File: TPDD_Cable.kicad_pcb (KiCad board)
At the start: 2 copper layers, 10.6 x 12 mm, 5 parts, among them J1 Wire Solder Pads, J2 TPDD, Q1 DTA114EKA, Q2 DTA114EKA, Q3 DTA114EKA

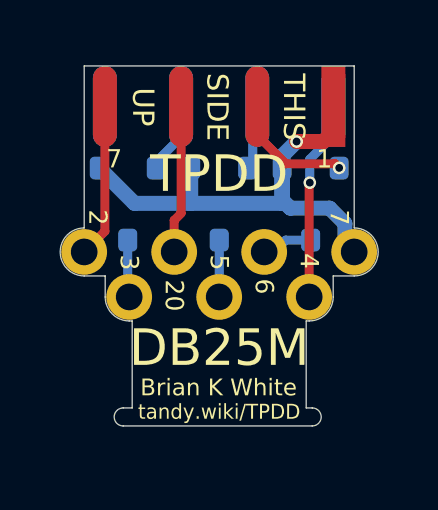
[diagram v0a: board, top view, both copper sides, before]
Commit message: pack v1 board tighter
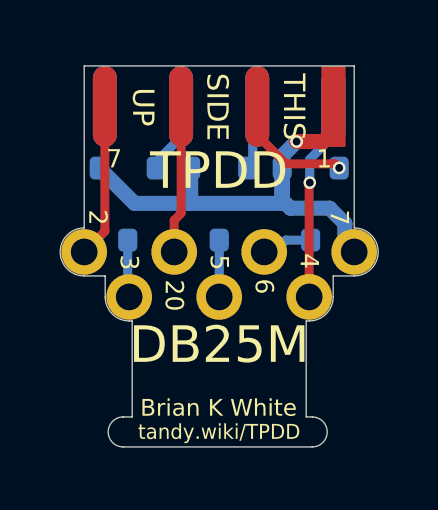
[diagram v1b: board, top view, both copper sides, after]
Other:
- board size 10.6 x 12 mm -> 10.6 x 12.7 mm
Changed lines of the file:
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@@
     (add_net /SG)
     (add_net /TX)
-    (add_net "Net-(J2-Pad8)")
   )
   (module 000_LOCAL:2-6-2_tpdd (layer Top)
@@
       (effects (font (size 1.2065 1.2065) (thickness 0.1016)) (justify right top mirror))
     )
+    (fp_line (start 0.762 1.524) (end 0.762 -1.516) (layer B.SilkS) (width 0.0508))
+    (fp_line (start -0.762 1.524) (end -0.762 -1.516) (layer B.SilkS) (width 0.0508))
+    (fp_line (start -0.762 1.524) (end 0.762 1.524) (layer B.SilkS) (width 0.0508))
     (fp_line (start -0.762 -1.516) (end 0.762 -1.516) (layer B.SilkS) (width 0.0508))
-    (fp_line (start -0.762 1.524) (end 0.762 1.524) (layer B.SilkS) (width 0.0508))
-    (fp_line (start -0.762 1.524) (end -0.762 -1.516) (layer B.SilkS) (width 0.0508))
-    (fp_line (start 0.762 1.524) (end 0.762 -1.516) (layer B.SilkS) (width 0.0508))
     (fp_text user %R (at 0 0) (layer B.Fab) hide
       (effects (font (size 0.5 0.5) (thickness 0.075)) (justify mirror))
@@
       (effects (font (size 1.2065 1.2065) (thickness 0.1016)) (justify right top mirror))
     )
+    (fp_line (start 0.762 1.524) (end 0.762 -1.516) (layer B.SilkS) (width 0.0508))
+    (fp_line (start -0.762 1.524) (end -0.762 -1.516) (layer B.SilkS) (width 0.0508))
+    (fp_line (start -0.762 1.524) (end 0.762 1.524) (layer B.SilkS) (width 0.0508))
     (fp_line (start -0.762 -1.516) (end 0.762 -1.516) (layer B.SilkS) (width 0.0508))
-    (fp_line (start -0.762 1.524) (end 0.762 1.524) (layer B.SilkS) (width 0.0508))
-    (fp_line (start -0.762 1.524) (end -0.762 -1.516) (layer B.SilkS) (width 0.0508))
-    (fp_line (start 0.762 1.524) (end 0.762 -1.516) (layer B.SilkS) (width 0.0508))
     (fp_text user %R (at 0 0) (layer B.Fab) hide
       (effects (font (size 0.5 0.5) (thickness 0.075)) (justify mirror))
@@
       (effects (font (size 1.2065 1.2065) (thickness 0.1016)) (justify right top mirror))
     )
+    (fp_line (start 0.762 1.524) (end 0.762 -1.516) (layer B.SilkS) (width 0.0508))
+    (fp_line (start -0.762 1.524) (end -0.762 -1.516) (layer B.SilkS) (width 0.0508))
+    (fp_line (start -0.762 1.524) (end 0.762 1.524) (layer B.SilkS) (width 0.0508))
     (fp_line (start -0.762 -1.516) (end 0.762 -1.516) (layer B.SilkS) (width 0.0508))
-    (fp_line (start -0.762 1.524) (end 0.762 1.524) (layer B.SilkS) (width 0.0508))
-    (fp_line (start -0.762 1.524) (end -0.762 -1.516) (layer B.SilkS) (width 0.0508))
-    (fp_line (start 0.762 1.524) (end 0.762 -1.516) (layer B.SilkS) (width 0.0508))
     (fp_text user %R (at 0 0) (layer B.Fab) hide
       (effects (font (size 0.5 0.5) (thickness 0.075)) (justify mirror))
@@
     )
   )
+  (gr_arc (start 148.093 93.1295) (end 148.093 93.6295) (angle -180) (layer Edge.Cuts) (width 0.0127))
+  (gr_arc (start 141.793 93.1295) (end 141.793 92.6295) (angle -180) (layer Edge.Cuts) (width 0.0127))
   (gr_line (start 149.493 86.3295) (end 149.493 80.9295) (layer Edge.Cuts) (width 0.0127))
   (gr_line (start 140.493 86.3295) (end 140.493 80.9295) (layer Edge.Cuts) (width 0.0127))
@@
   (gr_arc (start 140.493 87.1295) (end 140.493 86.3295) (angle -180) (layer Edge.Cuts) (width 0.0127))
   (gr_arc (start 149.493 87.1295) (end 149.493 87.9295) (angle -180) (layer Edge.Cuts) (width 0.0127))
-  (gr_line (start 147.893 92.3295) (end 147.893 89.4295) (layer Edge.Cuts) (width 0.0127))
-  (gr_line (start 142.093 92.3295) (end 142.093 89.4295) (layer Edge.Cuts) (width 0.0127))
-  (gr_line (start 142.093 92.3295) (end 141.793 92.3295) (layer Edge.Cuts) (width 0.0127))
-  (gr_line (start 147.893 92.3295) (end 148.093 92.3295) (layer Edge.Cuts) (width 0.0127))
-  (gr_arc (start 141.793 92.6295) (end 141.793 92.3295) (angle -180) (layer Edge.Cuts) (width 0.0127))
-  (gr_arc (start 148.093 92.6295) (end 148.093 92.9295) (angle -180) (layer Edge.Cuts) (width 0.0127))
+  (gr_line (start 147.893 92.6295) (end 147.893 89.4295) (layer Edge.Cuts) (width 0.0127))
+  (gr_line (start 142.093 92.6295) (end 142.093 89.4295) (layer Edge.Cuts) (width 0.0127))
+  (gr_line (start 142.093 92.6295) (end 141.793 92.6295) (layer Edge.Cuts) (width 0.0127))
+  (gr_line (start 147.893 92.6295) (end 148.093 92.6295) (layer Edge.Cuts) (width 0.0127))
   (gr_line (start 140.493 80.9295) (end 149.493 80.9295) (layer Edge.Cuts) (width 0.0127))
-  (gr_line (start 141.793 92.9295) (end 148.093 92.9295) (layer Edge.Cuts) (width 0.0127))
-  (gr_text tandy.wiki/TPDD (at 144.993 92.4595) (layer F.SilkS)
+  (gr_line (start 141.793 93.6295) (end 148.093 93.6295) (layer Edge.Cuts) (width 0.0127))
+  (gr_text tandy.wiki/TPDD (at 144.993 93.1295) (layer F.SilkS)
     (effects (font (size 0.5 0.48) (thickness 0.05)))
   )
@@
     (effects (font (size 0.7112 0.7112) (thickness 0.0762)))
   )
-  (gr_text Q1,Q2,Q3: (at 144.993 91.3295) (layer B.SilkS)
+  (gr_text Q1,Q2,Q3: (at 144.993 89.9295) (layer B.SilkS)
     (effects (font (size 0.7112 0.7112) (thickness 0.0762)) (justify mirror))
   )
@@
     (effects (font (size 0.7112 0.7112) (thickness 0.0762)) (justify mirror))
   )
-  (gr_text DTA114EKA (at 144.993 92.4795) (layer B.SilkS)
-    (effects (font (size 0.7112 0.7112) (thickness 0.0762)) (justify mirror))
-  )
-  (gr_text DB25M (at 144.993 90.3295) (layer F.SilkS)
+  (gr_text DTA114EKA (at 144.993 90.9295) (layer B.SilkS)
+    (effects (font (size 0.7112 0.7112) (thickness 0.0762)) (justify mirror))
+  )
+  (gr_text DB25M (at 144.993 90.2295) (layer F.SilkS)
     (effects (font (size 1.2192 1.2192) (thickness 0.1524)))
   )
-  (gr_text "Brian K White" (at 144.973 91.6495) (layer F.SilkS)
+  (gr_text "Brian K White" (at 144.973 92.3295) (layer F.SilkS)
     (effects (font (size 0.5588 0.5588) (thickness 0.0508)))
   )
@@
     (effects (font (size 0.6096 0.6096) (thickness 0.0762)))
   )
-  (gr_text TPDD (at 144.993 84.5295) (layer F.SilkS)
+  (gr_text TPDD (at 144.993 84.4295) (layer F.SilkS)
     (effects (font (size 1.2192 1.2192) (thickness 0.1524)))
   )

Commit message: cleanup
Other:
- board text added: "Q*: DTA114EKA"
- board text removed: "Brian K White"
- board text removed: "DTA114EKA"
- board text removed: "Q1,Q2,Q3:"
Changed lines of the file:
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@@
   (general
     (thickness 1.6)
-    (drawings 46)
+    (drawings 44)
     (tracks 48)
     (zones 0)
@@
       (effects (font (size 1.2065 1.2065) (thickness 0.1016)) (justify right top mirror))
     )
+    (fp_line (start -0.762 -1.516) (end 0.762 -1.516) (layer B.SilkS) (width 0.0508))
+    (fp_line (start -0.762 1.524) (end 0.762 1.524) (layer B.SilkS) (width 0.0508))
+    (fp_line (start -0.762 1.524) (end -0.762 -1.516) (layer B.SilkS) (width 0.0508))
     (fp_line (start 0.762 1.524) (end 0.762 -1.516) (layer B.SilkS) (width 0.0508))
-    (fp_line (start -0.762 1.524) (end -0.762 -1.516) (layer B.SilkS) (width 0.0508))
-    (fp_line (start -0.762 1.524) (end 0.762 1.524) (layer B.SilkS) (width 0.0508))
-    (fp_line (start -0.762 -1.516) (end 0.762 -1.516) (layer B.SilkS) (width 0.0508))
     (fp_text user %R (at 0 0) (layer B.Fab) hide
       (effects (font (size 0.5 0.5) (thickness 0.075)) (justify mirror))
@@
       (effects (font (size 1.2065 1.2065) (thickness 0.1016)) (justify right top mirror))
     )
+    (fp_line (start -0.762 -1.516) (end 0.762 -1.516) (layer B.SilkS) (width 0.0508))
+    (fp_line (start -0.762 1.524) (end 0.762 1.524) (layer B.SilkS) (width 0.0508))
+    (fp_line (start -0.762 1.524) (end -0.762 -1.516) (layer B.SilkS) (width 0.0508))
     (fp_line (start 0.762 1.524) (end 0.762 -1.516) (layer B.SilkS) (width 0.0508))
-    (fp_line (start -0.762 1.524) (end -0.762 -1.516) (layer B.SilkS) (width 0.0508))
-    (fp_line (start -0.762 1.524) (end 0.762 1.524) (layer B.SilkS) (width 0.0508))
-    (fp_line (start -0.762 -1.516) (end 0.762 -1.516) (layer B.SilkS) (width 0.0508))
     (fp_text user %R (at 0 0) (layer B.Fab) hide
       (effects (font (size 0.5 0.5) (thickness 0.075)) (justify mirror))
@@
       (effects (font (size 1.2065 1.2065) (thickness 0.1016)) (justify right top mirror))
     )
+    (fp_line (start -0.762 -1.516) (end 0.762 -1.516) (layer B.SilkS) (width 0.0508))
+    (fp_line (start -0.762 1.524) (end 0.762 1.524) (layer B.SilkS) (width 0.0508))
+    (fp_line (start -0.762 1.524) (end -0.762 -1.516) (layer B.SilkS) (width 0.0508))
     (fp_line (start 0.762 1.524) (end 0.762 -1.516) (layer B.SilkS) (width 0.0508))
-    (fp_line (start -0.762 1.524) (end -0.762 -1.516) (layer B.SilkS) (width 0.0508))
-    (fp_line (start -0.762 1.524) (end 0.762 1.524) (layer B.SilkS) (width 0.0508))
-    (fp_line (start -0.762 -1.516) (end 0.762 -1.516) (layer B.SilkS) (width 0.0508))
     (fp_text user %R (at 0 0) (layer B.Fab) hide
       (effects (font (size 0.5 0.5) (thickness 0.075)) (justify mirror))
@@
   (gr_line (start 141.793 93.6295) (end 148.093 93.6295) (layer Edge.Cuts) (width 0.0127))
   (gr_text tandy.wiki/TPDD (at 144.993 93.1295) (layer F.SilkS)
-    (effects (font (size 0.5 0.48) (thickness 0.05)))
+    (effects (font (size 0.55 0.55) (thickness 0.05)))
   )
   (gr_text THIS (at 147.483 82.296 -90) (layer F.SilkS)
@@
   (gr_text SIDE (at 144.9295 82.296 -90) (layer F.SilkS)
     (effects (font (size 0.7112 0.7112) (thickness 0.0762)))
-  )
-  (gr_text Q1,Q2,Q3: (at 144.993 89.9295) (layer B.SilkS)
-    (effects (font (size 0.7112 0.7112) (thickness 0.0762)) (justify mirror))
   )
   (gr_line (start 142.093 89.8295) (end 147.893 89.8295) (layer Dwgs.User) (width 0.0127))
@@
     (effects (font (size 0.7112 0.7112) (thickness 0.0762)) (justify mirror))
   )
-  (gr_text DTA114EKA (at 144.993 90.9295) (layer B.SilkS)
-    (effects (font (size 0.7112 0.7112) (thickness 0.0762)) (justify mirror))
+  (gr_text "Q*: DTA114EKA" (at 145.018 93.1295) (layer B.SilkS)
+    (effects (font (size 0.6 0.6) (thickness 0.05)) (justify mirror))
   )
   (gr_text DB25M (at 144.993 90.2295) (layer F.SilkS)
     (effects (font (size 1.2192 1.2192) (thickness 0.1524)))
   )
-  (gr_text "Brian K White" (at 144.973 92.3295) (layer F.SilkS)
-    (effects (font (size 0.5588 0.5588) (thickness 0.0508)))
-  )
   (gr_text DOWN (at 147.5584 82.4611 -270) (layer B.SilkS)
     (effects (font (size 0.7112 0.7112) (thickness 0.0762)) (justify mirror))
   )
-  (gr_text 4 (at 147.993 87.4295 -90) (layer F.SilkS)
-    (effects (font (size 0.6096 0.6096) (thickness 0.0762)))
-  )
-  (gr_text 5 (at 144.993 87.4795 -90) (layer F.SilkS)
-    (effects (font (size 0.6096 0.6096) (thickness 0.0762)))
-  )
-  (gr_text 3 (at 141.993 87.4795 -90) (layer F.SilkS)
-    (effects (font (size 0.6096 0.6096) (thickness 0.0762)))
-  )
-  (gr_text 2 (at 140.943 85.9795 -90) (layer F.SilkS)
-    (effects (font (size 0.6096 0.6096) (thickness 0.0762)))
-  )
-  (gr_text 20 (at 143.493 88.5795 -90) (layer F.SilkS)
-    (effects (font (size 0.6096 0.6096) (thickness 0.0762)))
-  )
-  (gr_text 6 (at 146.493 88.2795 -90) (layer F.SilkS)
-    (effects (font (size 0.6096 0.6096) (thickness 0.0762)))
-  )
-  (gr_text 7 (at 148.993 85.9795 -90) (layer F.SilkS)
-    (effects (font (size 0.6096 0.6096) (thickness 0.0762)))
-  )
+  (gr_text 4 (at 147.993 87.4045) (layer F.SilkS)
+    (effects (font (size 0.6096 0.6096) (thickness 0.0762)))
+  )
+  (gr_text 5 (at 144.993 87.4045) (layer F.SilkS)
+    (effects (font (size 0.6096 0.6096) (thickness 0.0762)))
+  )
+  (gr_text 3 (at 141.993 87.4045) (layer F.SilkS)
+    (effects (font (size 0.6096 0.6096) (thickness 0.0762)))
+  )
+  (gr_text 2 (at 140.793 85.9045) (layer F.SilkS)
+    (effects (font (size 0.6096 0.6096) (thickness 0.0762)))
+  )
+  (gr_text 20 (at 143.493 85.9045) (layer F.SilkS)
+    (effects (font (size 0.6096 0.6096) (thickness 0.0762)))
+  )
+  (gr_text 6 (at 146.493 85.9045) (layer F.SilkS)
+    (effects (font (size 0.6096 0.6096) (thickness 0.0762)))
+  )
+  (gr_text 7 (at 149.218 85.9545) (layer F.SilkS)
+    (effects (font (size 0.6096 0.6096) (thickness 0.0762)))
+  )
